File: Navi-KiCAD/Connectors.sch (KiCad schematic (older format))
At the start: 7 parts, among them J4 473460001, J5 AXK5S80047YG, J6 AXK5S80047YG, U13 NUF2042XV6T1G

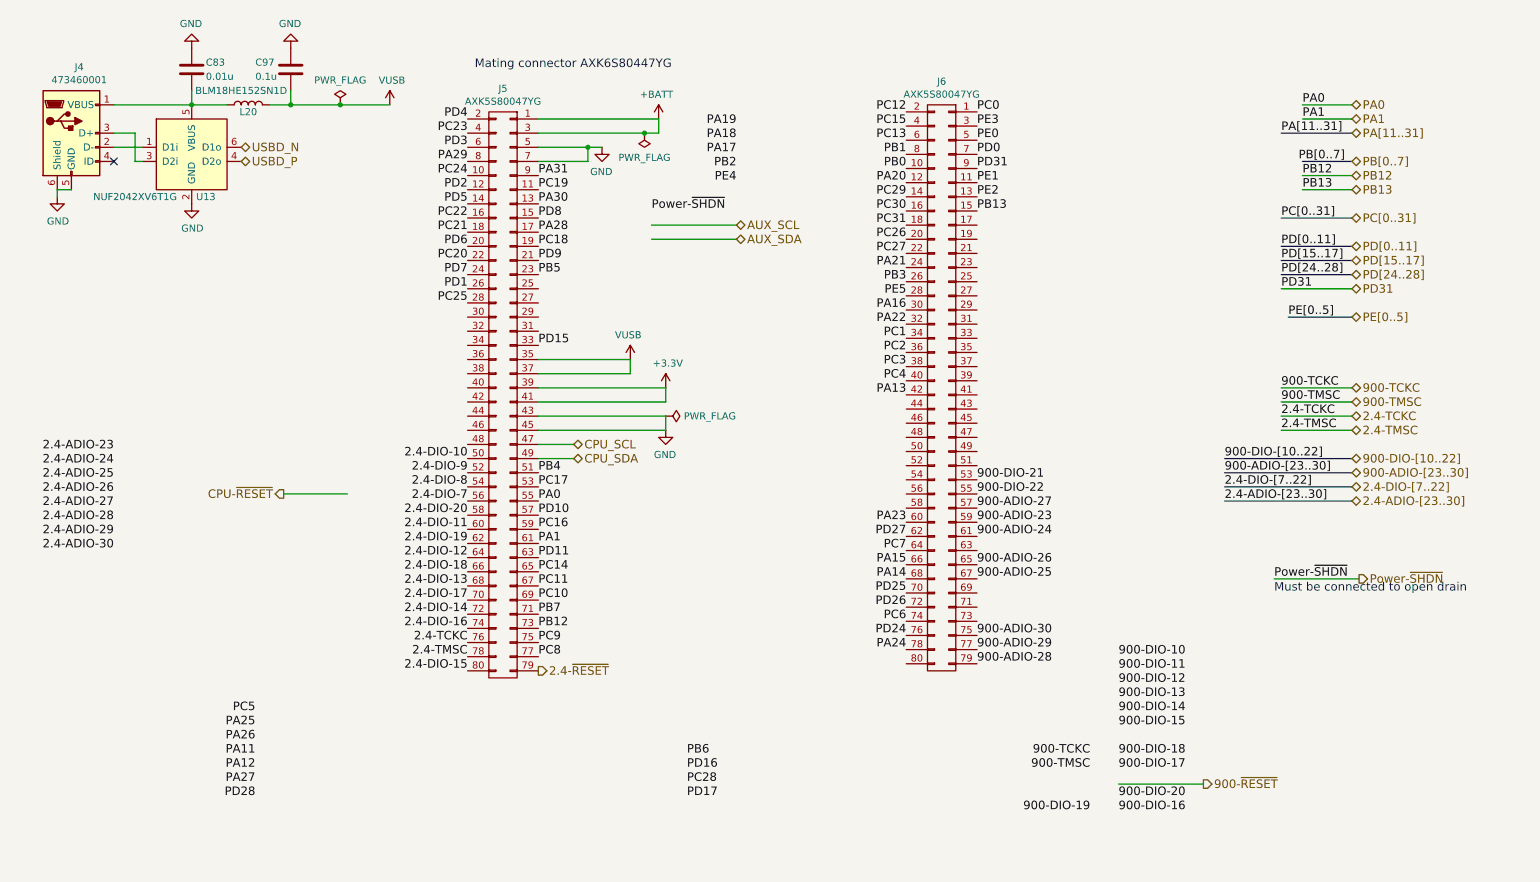
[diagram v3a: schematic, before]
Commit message: Upgraded to 9 channel RGB driver. Broke out signals for LSM303 and LSM6DS3
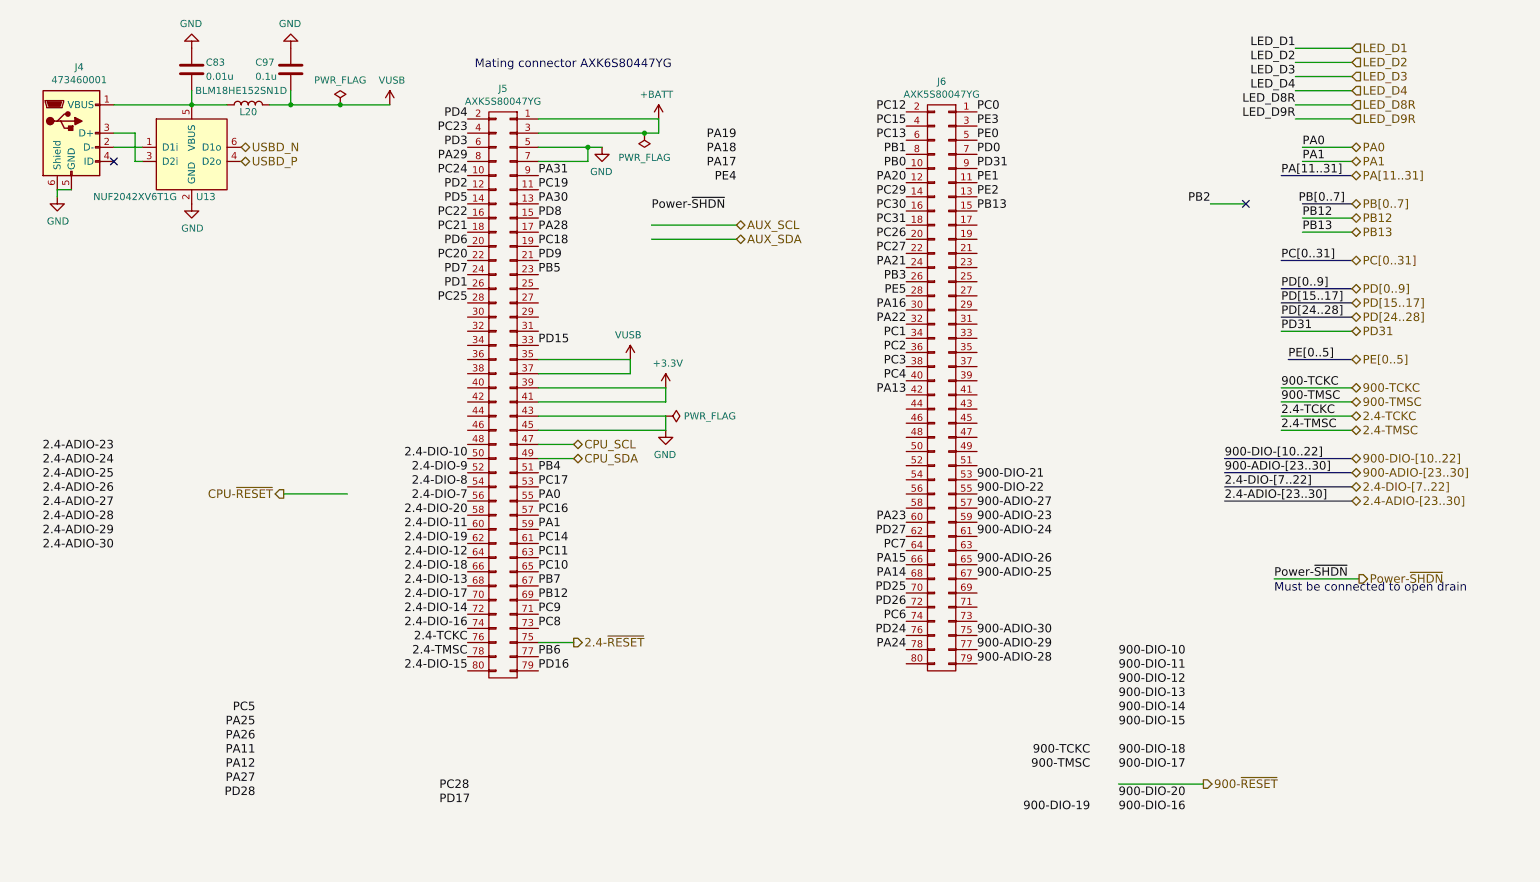
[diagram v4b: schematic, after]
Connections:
- net labels added: LED_D1, LED_D2, LED_D3, LED_D4, LED_D8R, LED_D9R, PD[0..9]
- net labels removed: PD10, PD11, PD[0..11]
- wire segments 42 -> 50
- no-connect marks 1 -> 2
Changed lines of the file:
@@
 $Descr A4 11693 8268
 encoding utf-8
-Sheet 8 8
+Sheet 7 8
 Title ""
 Date ""
@@
 $EndComp
 $Comp
-L VUSB #PWR0154
+L VUSB #PWR110
 U 1 1 58B8BBBA
 P 3200 1300
-F 0 "#PWR0154" H 1200 -100 50  0001 C CNN
+F 0 "#PWR110" H 1200 -100 50  0001 C CNN
 F 1 "VUSB" H 3215 1473 50  0000 C CNN
 F 2 "" H 1200 50  50  0001 C CNN
@@
 $EndComp
 $Comp
-L GND #PWR0155
+L GND #PWR106
 U 1 1 58B8BD69
 P 850 1950
-F 0 "#PWR0155" H -1050 100 50  0001 C CNN
+F 0 "#PWR106" H -1050 100 50  0001 C CNN
 F 1 "GND" H 855 1777 50  0000 C CNN
 F 2 "" H -1050 350 50  0001 C CNN
@@
 Text HLabel 8950 6100 2    60   Output ~ 0
 900-~RESET
-Text HLabel 4250 5300 2    60   Output ~ 0
+Text HLabel 4500 5100 2    60   Output ~ 0
 2.4-~RESET
-Text HLabel 10000 2100 2    60   BiDi ~ 0
+Text HLabel 10000 2400 2    60   BiDi ~ 0
 PC[0..31]
-Wire Bus Line
-	10000 2100 9500 2100
-Text Label 9500 2100 0    60   ~ 0
-PC[0..31]
-Text HLabel 10000 2300 2    60   BiDi ~ 0
-PD[0..11]
-Wire Bus Line
-	10000 2300 9500 2300
-Text Label 9500 2300 0    60   ~ 0
-PD[0..11]
-Text HLabel 10000 2400 2    60   BiDi ~ 0
-PD[15..17]
 Wire Bus Line
 	10000 2400 9500 2400
 Text Label 9500 2400 0    60   ~ 0
+PC[0..31]
+Text HLabel 10000 2600 2    60   BiDi ~ 0
+PD[0..9]
+Wire Bus Line
+	10000 2600 9500 2600
+Text Label 9500 2600 0    60   ~ 0
+PD[0..9]
+Text HLabel 10000 2700 2    60   BiDi ~ 0
 PD[15..17]
-Text HLabel 10000 2500 2    60   BiDi ~ 0
+Wire Bus Line
+	10000 2700 9500 2700
+Text Label 9500 2700 0    60   ~ 0
+PD[15..17]
+Text HLabel 10000 2800 2    60   BiDi ~ 0
 PD[24..28]
 Wire Bus Line
-	10000 2500 9500 2500
-Text Label 9500 2500 0    60   ~ 0
+	10000 2800 9500 2800
+Text Label 9500 2800 0    60   ~ 0
 PD[24..28]
-Text HLabel 10000 2800 2    60   BiDi ~ 0
+Text HLabel 10000 3100 2    60   BiDi ~ 0
 PE[0..5]
 Wire Bus Line
-	10000 2800 9550 2800
-Text Label 9550 2800 0    60   ~ 0
+	10000 3100 9550 3100
+Text Label 9550 3100 0    60   ~ 0
 PE[0..5]
-Text Label 9500 2600 0    60   ~ 0
+Text Label 9500 2900 0    60   ~ 0
 PD31
-Text HLabel 10000 2600 2    60   BiDi ~ 0
+Text HLabel 10000 2900 2    60   BiDi ~ 0
 PD31
 Text HLabel 5650 2250 2    60   BiDi ~ 0
@@
 Text HLabel 4500 3700 2    60   BiDi ~ 0
 CPU_SCL
-Text HLabel 10000 1500 2    60   BiDi ~ 0
+Text HLabel 10000 1800 2    60   BiDi ~ 0
 PA[11..31]
 Wire Bus Line
-	10000 1500 9500 1500
-Text Label 9500 1500 0    60   ~ 0
+	10000 1800 9500 1800
+Text Label 9500 1800 0    60   ~ 0
 PA[11..31]
-Text HLabel 10000 1300 2    60   BiDi ~ 0
+Text HLabel 10000 1600 2    60   BiDi ~ 0
 PA0
-Text HLabel 10000 1400 2    60   BiDi ~ 0
+Text HLabel 10000 1700 2    60   BiDi ~ 0
 PA1
-Text HLabel 10000 1700 2    60   BiDi ~ 0
+Text HLabel 10000 2000 2    60   BiDi ~ 0
 PB[0..7]
-Text HLabel 10000 1900 2    60   BiDi ~ 0
+Text HLabel 10000 2200 2    60   BiDi ~ 0
 PB13
-Text HLabel 10000 1800 2    60   BiDi ~ 0
+Text HLabel 10000 2100 2    60   BiDi ~ 0
 PB12
 Wire Bus Line
-	10000 1700 9650 1700
-Text Label 9950 1700 2    60   ~ 0
+	10000 2000 9650 2000
+Text Label 9950 2000 2    60   ~ 0
 PB[0..7]
 Wire Wire Line
@@
 Must be connected to open drain\n
 $Comp
-L +BATT #PWR0156
+L +BATT #PWR113
 U 1 1 58DB91A4
 P 5100 1400
-F 0 "#PWR0156" H 4050 -1500 50  0001 C CNN
+F 0 "#PWR113" H 4050 -1500 50  0001 C CNN
 F 1 "+BATT" H 5115 1573 50  0000 C CNN
 F 2 "" H 4050 -1350 50  0001 C CNN
@@
 $EndComp
 Wire Wire Line
-	9500 2600 10000 2600
-$Comp
-L GND #PWR0157
+	9500 2900 10000 2900
+$Comp
+L GND #PWR111
 U 1 1 58DD26EA
 P 4700 1600
-F 0 "#PWR0157" H 750 -2100 50  0001 C CNN
+F 0 "#PWR111" H 750 -2100 50  0001 C CNN
 F 1 "GND" H 4705 1427 50  0000 C CNN
 F 2 "" H 750 -1850 50  0001 C CNN
@@
 Text Label 1250 4450 2    60   ~ 0
 2.4-ADIO-30
-Text Label 5300 6200 0    60   ~ 0
+Text Label 3550 6250 0    60   ~ 0
 PD17
-Text Label 5300 6100 0    60   ~ 0
+Text Label 3550 6150 0    60   ~ 0
 PC28
 Wire Wire Line
 	4250 3700 4500 3700
-Text Label 5300 6000 0    60   ~ 0
+Text Label 4250 5300 0    60   ~ 0
 PD16
-Text Label 4250 5200 0    60   ~ 0
+Text Label 4250 5000 0    60   ~ 0
 PC8
-Text Label 4250 5100 0    60   ~ 0
+Text Label 4250 4900 0    60   ~ 0
 PC9
-Text Label 4250 4900 0    60   ~ 0
+Text Label 4250 4700 0    60   ~ 0
 PB7
-Text Label 4250 4800 0    60   ~ 0
+Text Label 4250 4600 0    60   ~ 0
 PC10
 Wire Wire Line
 	4500 3800 4250 3800
-Text Label 4250 4600 0    60   ~ 0
+Text Label 4250 4400 0    60   ~ 0
 PC14
-Text Label 4250 4500 0    60   ~ 0
-PD11
-Text Label 4250 4400 0    60   ~ 0
+Text Label 4250 4300 0    60   ~ 0
 PA1
-Text Label 4250 4300 0    60   ~ 0
+Text Label 4250 4200 0    60   ~ 0
 PC16
-Text Label 4250 4200 0    60   ~ 0
-PD10
 Text Label 4250 4100 0    60   ~ 0
 PA0
@@
 Text Label 3750 4100 2    60   ~ 0
 2.4-DIO-7
-Text Label 5300 5900 0    60   ~ 0
+Text Label 4250 5200 0    60   ~ 0
 PB6
-Text Label 4250 4700 0    60   ~ 0
+Text Label 4250 4500 0    60   ~ 0
 PC11
 Text Label 4250 2100 0    60   ~ 0
@@
 Text Label 6850 1850 2    60   ~ 0
 PA20
-Text Label 5650 1450 2    60   ~ 0
+Text Label 5650 1550 2    60   ~ 0
 PA19
-Text Label 5650 1550 2    60   ~ 0
+Text Label 5650 1650 2    60   ~ 0
 PA18
-Text Label 5650 1650 2    60   ~ 0
+Text Label 5650 1750 2    60   ~ 0
 PA17
-Text Label 5650 1750 2    60   ~ 0
+Text Label 9000 2000 2    60   ~ 0
 PB2
 Text Label 5650 1850 2    60   ~ 0
@@
 PA15
 Wire Wire Line
-	9650 1800 10000 1800
-Wire Wire Line
-	10000 1900 9650 1900
-Wire Wire Line
-	10000 1400 9650 1400
-Wire Wire Line
-	10000 1300 9650 1300
-Text Label 9650 1300 0    60   ~ 0
+	9650 2100 10000 2100
+Wire Wire Line
+	10000 2200 9650 2200
+Wire Wire Line
+	10000 1700 9650 1700
+Wire Wire Line
+	10000 1600 9650 1600
+Text Label 9650 1600 0    60   ~ 0
 PA0
-Text Label 9650 1400 0    60   ~ 0
+Text Label 9650 1700 0    60   ~ 0
 PA1
-Text Label 9650 1800 0    60   ~ 0
+Text Label 9650 2100 0    60   ~ 0
 PB12
-Text Label 9650 1900 0    60   ~ 0
+Text Label 9650 2200 0    60   ~ 0
 PB13
-Text Label 4250 5000 0    60   ~ 0
+Text Label 4250 4800 0    60   ~ 0
 PB12
 Text Label 5050 2050 0    60   ~ 0
@@
 	4250 3400 5150 3400
 $Comp
-L GND #PWR0158
+L GND #PWR115
 U 1 1 58BDD19A
 P 5150 3600
-F 0 "#PWR0158" H 1200 -100 50  0001 C CNN
+F 0 "#PWR115" H 1200 -100 50  0001 C CNN
 F 1 "GND" H 5155 3427 50  0000 C CNN
 F 2 "" H 1200 150 50  0001 C CNN
@@
 	4250 3200 4900 3200
 $Comp
-L PWR_FLAG #FLG0159
+L PWR_FLAG #FLG16
 U 1 1 58BE5320
 P 5000 1500
-F 0 "#FLG0159" H -650 75  50  0001 C CNN
+F 0 "#FLG16" H -650 75  50  0001 C CNN
 F 1 "PWR_FLAG" H 5000 1673 50  0000 C CNN
 F 2 "" H -650 0   50  0001 C CNN
@@
 Connection ~ 5000 1500
 $Comp
-L PWR_FLAG #FLG0160
+L PWR_FLAG #FLG15
 U 1 1 58BE5430
 P 2850 1300
-F 0 "#FLG0160" H -2800 -125 50  0001 C CNN
+F 0 "#FLG15" H -2800 -125 50  0001 C CNN
 F 1 "PWR_FLAG" H 2850 1474 50  0000 C CNN
 F 2 "" H -2800 -200 50  0001 C CNN
@@
 $EndComp
 $Comp
-L PWR_FLAG #FLG0161
+L PWR_FLAG #FLG17
 U 1 1 58BEF4A7
 P 5150 3500
-F 0 "#FLG0161" H -500 2075 50  0001 C CNN
+F 0 "#FLG17" H -500 2075 50  0001 C CNN
 F 1 "PWR_FLAG" V 5150 3628 50  0000 L CNN
 F 2 "" H -500 2000 50  0001 C CNN
@@
 	4900 3200 4900 3100
 $Comp
-L +3.3V #PWR0162
+L +3.3V #PWR114
 U 1 1 58BFD1FD
 P 5150 3300
-F 0 "#PWR0162" H 2150 1200 50  0001 C CNN
+F 0 "#PWR114" H 2150 1200 50  0001 C CNN
 F 1 "+3.3V" H 5165 3473 50  0000 C CNN
 F 2 "" H 2150 1350 50  0001 C CNN
@@
 	5150 3400 5150 3300
 $Comp
-L VUSB #PWR0163
+L VUSB #PWR112
 U 1 1 58E3762E
 P 4900 3100
-F 0 "#PWR0163" H 2900 1700 50  0001 C CNN
+F 0 "#PWR112" H 2900 1700 50  0001 C CNN
 F 1 "VUSB" H 4915 3273 50  0000 C CNN
 F 2 "" H 2900 1850 50  0001 C CNN
@@
 $EndComp
 $Comp
-L GND #PWR0164
+L GND #PWR108
 U 1 1 58E380BC
 P 1800 2000
-F 0 "#PWR0164" H -100 150 50  0001 C CNN
+F 0 "#PWR108" H -100 150 50  0001 C CNN
 F 1 "GND" H 1805 1827 50  0000 C CNN
 F 2 "" H -100 400 50  0001 C CNN
@@
 Connection ~ 2850 1300
 $Comp
-L GND #PWR0165
+L GND #PWR107
 U 1 1 58CFD68A
 P 1800 900
-F 0 "#PWR0165" H -100 -950 50  0001 C CNN
+F 0 "#PWR107" H -100 -950 50  0001 C CNN
 F 1 "GND" H 1805 727 50  0000 C CNN
 F 2 "" H -100 -700 50  0001 C CNN
@@
 $EndComp
 $Comp
-L GND #PWR0166
+L GND #PWR109
 U 1 1 58CFD6F1
 P 2500 900
-F 0 "#PWR0166" H 600 -950 50  0001 C CNN
+F 0 "#PWR109" H 600 -950 50  0001 C CNN
 F 1 "GND" H 2505 727 50  0000 C CNN
 F 2 "" H 600 -700 50  0001 C CNN
@@
 	2500 1300 2500 1200
 Connection ~ 2500 1300
+Wire Wire Line
+	9000 2000 9250 2000
+NoConn ~ 9250 2000
+Wire Wire Line
+	4250 5100 4500 5100
+Text Label 9600 900  2    60   ~ 0
+LED_D1
+Text Label 9600 1000 2    60   ~ 0
+LED_D2
+Text Label 9600 1100 2    60   ~ 0
+LED_D3
+Text Label 9600 1200 2    60   ~ 0
+LED_D4
+Text Label 9600 1300 2    60   ~ 0
+LED_D8R
+Text Label 9600 1400 2    60   ~ 0
+LED_D9R
+Text HLabel 10000 900  2    60   Input ~ 0
+LED_D1
+Wire Wire Line
+	10000 900  9600 900
+Text HLabel 10000 1000 2    60   Input ~ 0
+LED_D2
+Wire Wire Line
+	10000 1000 9600 1000
+Text HLabel 10000 1100 2    60   Input ~ 0
+LED_D3
+Wire Wire Line
+	10000 1100 9600 1100
+Text HLabel 10000 1200 2    60   Input ~ 0
+LED_D4
+Wire Wire Line
+	10000 1200 9600 1200
+Text HLabel 10000 1300 2    60   Input ~ 0
+LED_D8R
+Wire Wire Line
+	10000 1300 9600 1300
+Text HLabel 10000 1400 2    60   Input ~ 0
+LED_D9R
+Wire Wire Line
+	10000 1400 9600 1400
 $EndSCHEMATC

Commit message: Tweaked pinouts and finished routing known connectors. Now for the remaining IO.
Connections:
- wire segments 50 -> 52
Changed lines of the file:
@@
 $EndComp
 $Comp
-L VUSB #PWR121
+L VUSB #PWR0132
 U 1 1 58B8BBBA
 P 3200 1300
-F 0 "#PWR121" H 1200 -100 50  0001 C CNN
+F 0 "#PWR0132" H 1200 -100 50  0001 C CNN
 F 1 "VUSB" H 3215 1473 50  0000 C CNN
 F 2 "" H 1200 50  50  0001 C CNN
@@
 $EndComp
 $Comp
-L GND #PWR117
+L GND #PWR0133
 U 1 1 58B8BD69
 P 850 1950
-F 0 "#PWR117" H -1050 100 50  0001 C CNN
+F 0 "#PWR0133" H -1050 100 50  0001 C CNN
 F 1 "GND" H 855 1777 50  0000 C CNN
 F 2 "" H -1050 350 50  0001 C CNN
@@
 Must be connected to open drain\n
 $Comp
-L +BATT #PWR124
+L +BATT #PWR0134
 U 1 1 58DB91A4
 P 5100 1400
-F 0 "#PWR124" H 4050 -1500 50  0001 C CNN
+F 0 "#PWR0134" H 4050 -1500 50  0001 C CNN
 F 1 "+BATT" H 5115 1573 50  0000 C CNN
 F 2 "" H 4050 -1350 50  0001 C CNN
@@
 	9500 2900 10000 2900
 $Comp
-L GND #PWR122
+L GND #PWR0135
 U 1 1 58DD26EA
 P 4700 1600
-F 0 "#PWR122" H 750 -2100 50  0001 C CNN
+F 0 "#PWR0135" H 750 -2100 50  0001 C CNN
 F 1 "GND" H 4705 1427 50  0000 C CNN
 F 2 "" H 750 -1850 50  0001 C CNN
@@
 Text Label 3750 4200 2    60   ~ 0
 2.4-DIO-20
-Text Label 1250 3750 2    60   ~ 0
+Text Label 4250 2700 0    60   ~ 0
 2.4-ADIO-23
-Text Label 1250 3850 2    60   ~ 0
+Text Label 4250 2600 0    60   ~ 0
 2.4-ADIO-24
-Text Label 1250 3950 2    60   ~ 0
+Text Label 4250 2800 0    60   ~ 0
 2.4-ADIO-25
 Text Label 1250 4050 2    60   ~ 0
@@
 Text Label 1250 4350 2    60   ~ 0
 2.4-ADIO-29
-Text Label 1250 4450 2    60   ~ 0
+Text Label 4250 2900 0    60   ~ 0
 2.4-ADIO-30
 Text Label 3550 6250 0    60   ~ 0
@@
 Text Label 5650 1750 2    60   ~ 0
 PA17
-Text Label 9000 2000 2    60   ~ 0
+Text Label 5650 1450 2    60   ~ 0
 PB2
 Text Label 5650 1850 2    60   ~ 0
@@
 Text Label 6850 2750 2    60   ~ 0
 PA16
-Text Label 8150 5900 2    60   ~ 0
+Text Label 7350 4850 0    60   ~ 0
 900-TCKC
-Text Label 8150 6000 2    60   ~ 0
+Text Label 7350 4750 0    60   ~ 0
 900-TMSC
+Text Label 6850 4150 2    60   ~ 0
+PA23
+Text Label 7750 750  2    60   ~ 0
+PD27
 Text Label 6850 4250 2    60   ~ 0
-PA23
-Text Label 6850 4350 2    60   ~ 0
-PD27
-Text Label 6850 4450 2    60   ~ 0
 PC7
 Wire Wire Line
@@
 	5100 1500 5100 1400
 Connection ~ 4600 1600
-Text Label 8350 5200 0    60   ~ 0
+Text Label 6850 5050 2    60   ~ 0
 900-DIO-10
-Text Label 8350 5300 0    60   ~ 0
+Text Label 6850 5150 2    60   ~ 0
 900-DIO-11
-Text Label 8350 5400 0    60   ~ 0
+Text Label 6850 5250 2    60   ~ 0
 900-DIO-12
-Text Label 8350 5500 0    60   ~ 0
+Text Label 7350 4950 0    60   ~ 0
 900-DIO-13
 Text Label 8350 5600 0    60   ~ 0
 900-DIO-14
-Text Label 8350 5700 0    60   ~ 0
+Text Label 7350 4450 0    60   ~ 0
 900-DIO-15
 Wire Wire Line
@@
 Text Label 2250 5600 2    60   ~ 0
 PC5
-Text Label 6850 5150 2    60   ~ 0
+Text Label 6850 4950 2    60   ~ 0
 PA24
-Text Label 6850 5050 2    60   ~ 0
+Text Label 6850 4850 2    60   ~ 0
 PD24
-Text Label 6850 4950 2    60   ~ 0
+Text Label 6850 4750 2    60   ~ 0
 PC6
-Text Label 6850 4850 2    60   ~ 0
+Text Label 6850 4650 2    60   ~ 0
 PD26
-Text Label 6850 4750 2    60   ~ 0
+Text Label 6850 4550 2    60   ~ 0
 PD25
-Text Label 6850 4650 2    60   ~ 0
+Text Label 6850 4450 2    60   ~ 0
 PA14
-Text Label 6850 4550 2    60   ~ 0
+Text Label 6850 4350 2    60   ~ 0
 PA15
 Wire Wire Line
@@
 	4250 3400 5150 3400
 $Comp
-L GND #PWR126
+L GND #PWR0136
 U 1 1 58BDD19A
 P 5150 3600
-F 0 "#PWR126" H 1200 -100 50  0001 C CNN
+F 0 "#PWR0136" H 1200 -100 50  0001 C CNN
 F 1 "GND" H 5155 3427 50  0000 C CNN
 F 2 "" H 1200 150 50  0001 C CNN
@@
 	4250 3200 4900 3200
 $Comp
-L PWR_FLAG #FLG17
+L PWR_FLAG #FLG0137
 U 1 1 58BE5320
 P 5000 1500
-F 0 "#FLG17" H -650 75  50  0001 C CNN
+F 0 "#FLG0137" H -650 75  50  0001 C CNN
 F 1 "PWR_FLAG" H 5000 1673 50  0000 C CNN
 F 2 "" H -650 0   50  0001 C CNN
@@
 Connection ~ 5000 1500
 $Comp
-L PWR_FLAG #FLG16
+L PWR_FLAG #FLG0138
 U 1 1 58BE5430
 P 2850 1300
-F 0 "#FLG16" H -2800 -125 50  0001 C CNN
+F 0 "#FLG0138" H -2800 -125 50  0001 C CNN
 F 1 "PWR_FLAG" H 2850 1474 50  0000 C CNN
 F 2 "" H -2800 -200 50  0001 C CNN
@@
 $EndComp
 $Comp
-L PWR_FLAG #FLG18
+L PWR_FLAG #FLG0139
 U 1 1 58BEF4A7
 P 5150 3500
-F 0 "#FLG18" H -500 2075 50  0001 C CNN
+F 0 "#FLG0139" H -500 2075 50  0001 C CNN
 F 1 "PWR_FLAG" V 5150 3628 50  0000 L CNN
 F 2 "" H -500 2000 50  0001 C CNN
@@
 	4900 3200 4900 3100
 $Comp
-L +3.3V #PWR125
+L +3.3V #PWR0140
 U 1 1 58BFD1FD
 P 5150 3300
-F 0 "#PWR125" H 2150 1200 50  0001 C CNN
+F 0 "#PWR0140" H 2150 1200 50  0001 C CNN
 F 1 "+3.3V" H 5165 3473 50  0000 C CNN
 F 2 "" H 2150 1350 50  0001 C CNN
@@
 	5150 3400 5150 3300
 $Comp
-L VUSB #PWR123
+L VUSB #PWR0141
 U 1 1 58E3762E
 P 4900 3100
-F 0 "#PWR123" H 2900 1700 50  0001 C CNN
+F 0 "#PWR0141" H 2900 1700 50  0001 C CNN
 F 1 "VUSB" H 4915 3273 50  0000 C CNN
 F 2 "" H 2900 1850 50  0001 C CNN
@@
 $EndComp
 $Comp
-L GND #PWR119
+L GND #PWR0142
 U 1 1 58E380BC
 P 1800 2000
-F 0 "#PWR119" H -100 150 50  0001 C CNN
+F 0 "#PWR0142" H -100 150 50  0001 C CNN
 F 1 "GND" H 1805 1827 50  0000 C CNN
 F 2 "" H -100 400 50  0001 C CNN
@@
 Connection ~ 2850 1300
 $Comp
-L GND #PWR118
+L GND #PWR0143
 U 1 1 58CFD68A
 P 1800 900
-F 0 "#PWR118" H -100 -950 50  0001 C CNN
+F 0 "#PWR0143" H -100 -950 50  0001 C CNN
 F 1 "GND" H 1805 727 50  0000 C CNN
 F 2 "" H -100 -700 50  0001 C CNN
@@
 $EndComp
 $Comp
-L GND #PWR120
+L GND #PWR0144
 U 1 1 58CFD6F1
 P 2500 900
-F 0 "#PWR120" H 600 -950 50  0001 C CNN
+F 0 "#PWR0144" H 600 -950 50  0001 C CNN
 F 1 "GND" H 2505 727 50  0000 C CNN
 F 2 "" H 600 -700 50  0001 C CNN
@@
 Connection ~ 2500 1300
 Wire Wire Line
-	9000 2000 9250 2000
-NoConn ~ 9250 2000
+	5650 1450 5900 1450
 Wire Wire Line
 	4250 5100 4500 5100
@@
 Wire Wire Line
 	10000 1400 9600 1400
+Wire Wire Line
+	7750 750  7450 750
+Wire Wire Line
+	7450 750  7450 800
+NoConn ~ 7450 800
 $EndSCHEMATC
